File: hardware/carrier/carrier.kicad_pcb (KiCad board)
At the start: 2 copper layers, 117.9 x 72.3 mm, 18 parts, among them J1 12V pigtail, U1 D1 Mini ESP32 (Type-C), U2 PCA9685 16ch servo, U3 LM2596 buck 12V->5.05V

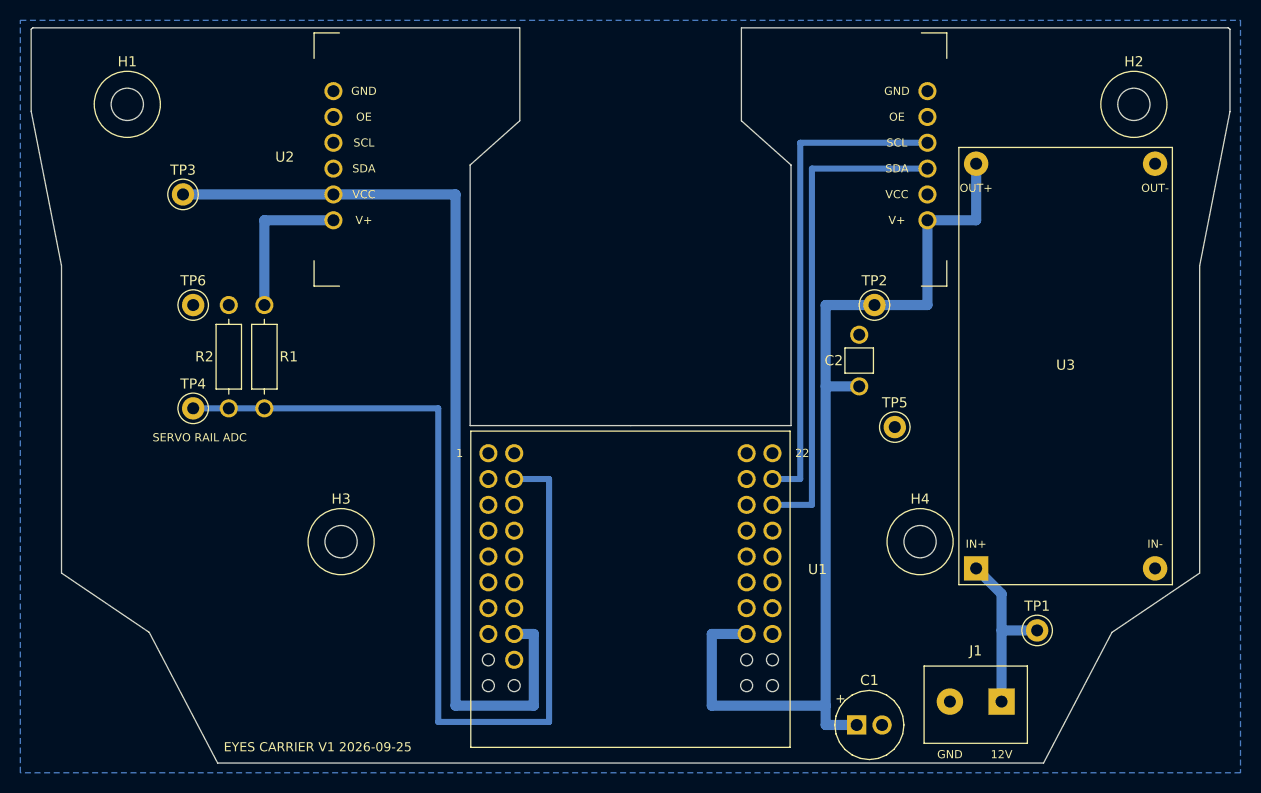
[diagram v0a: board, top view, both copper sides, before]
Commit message: carrier V2: Scott's placement captured, outline restored, divider dropped, DRC 0
PCA on H3/H4 (its holes match the carrier's), D1 Mini in the left wing
with USB-C off the left edge, buck in the right wing, servo headers on
the bottom edge. No routing yet; V1's tracks belonged to the rejected
placement and are gone.

Why a capture step (gen/capture_placement.py -> placement.py) instead of
making the .kicad_pcb the master: the GUI-only path broke the outline
within one session (loose Edge.Cuts lines move under box-select) and
placed three parts off the real board. Regenerating keeps the DXF
outline, hole keepouts and D1 keepouts correct by construction.

Why the hole footprint lost its courtyard and silk ring, and the PCA
courtyard shrank to its header rows: the holes sit inside the PCA by
design; every DRC courtyard check was describing the intent.

Why solid pour connections on U2 pins 6/12 and U3 pins 2/4: servo and
buck return current, and the H3/H4 keepout leaves the PCA GND pins a
single 0.5 mm spoke. Everything else keeps thermal reliefs.

Why min_resolved_spokes 1: the D1's inner GND pin can only be reached
from the module middle; its other two GND pins carry the return.

Rail divider (R1/R2/TP4) removed per Scott: the ADC measured its own
noise, not sag.

Co-Authored-By: Claude Fable 5.1 <noreply@anthropic.com>
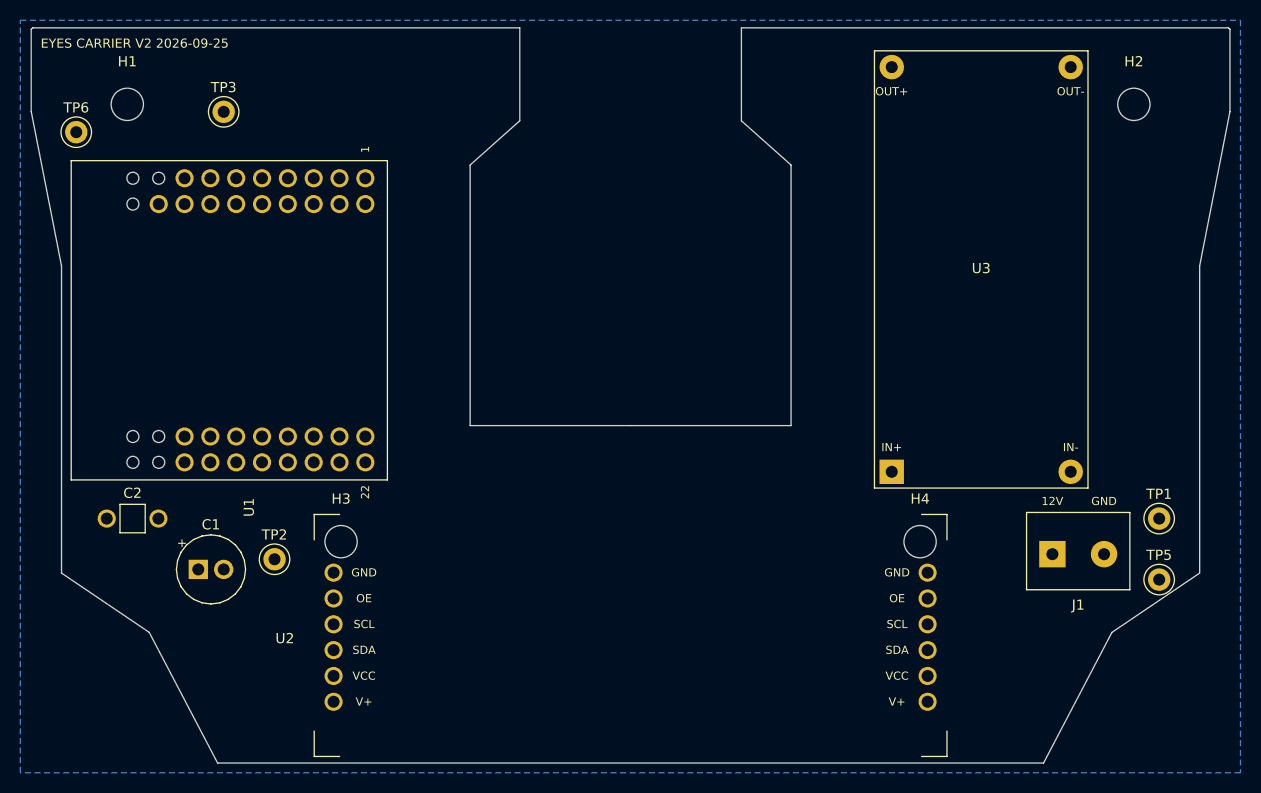
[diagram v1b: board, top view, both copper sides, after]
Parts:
- removed the H4 at (128.5, 115.3)
- removed R1, R2: 10k, carrier:R_Axial_P10.16
- removed the U1 at (100.0, 118.0)
- added U2: PCA9685 16ch servo, carrier:PCA9685_Adafruit_Module, F.Cu at (100.0, 124.8)
- H4: renamed from TP4; value RAIL_ADC -> M3 rack standoff; footprint carrier:TestPoint_THT_D2.2_1.181 -> carrier:MountingHole_M3_3.175
- U1: renamed from U2; value PCA9685 16ch servo -> D1 Mini ESP32 (Type-C); footprint carrier:PCA9685_Adafruit_Module -> carrier:D1_Mini_ESP32_THT
- moved C2 75.1 mm to (48.5, 113.0), turned to 0 degrees
- moved H4 72.7 mm to (128.5, 115.3)
- moved C1 66.5 mm to (57.5, 118.0)
- moved TP2 64.1 mm to (65.0, 117.0)
- moved U1 40.8 mm to (62.5, 93.5), turned to -90 degrees
- moved TP5 30.0 mm to (152.0, 119.0)
- moved TP6 20.5 mm to (45.5, 75.0)
- moved TP1 16.3 mm to (152.0, 113.0)
- moved J1 15.3 mm to (141.5, 116.5), turned to 0 degrees
- moved U3 12.6 mm to (143.3, 108.4)
- moved TP3 9.05 mm to (60.0, 73.0)
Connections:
- U1 pad 1: +5V -> GND
- U1 pad 10: SCL -> (no net)
- U1 pad 12: GND -> (no net)
- U1 pad 2: +3V3 -> (no net)
- U1 pad 6: GND -> (no net)
- U1 pad 7: +5V -> (no net)
- U1 pad 9: SDA -> (no net)
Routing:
- net +5V: track 113.2 -> 0.00 mm
- net +3V3: track 93.8 -> 0.00 mm
- net RAIL_ADC: track 93.2 -> 0.00 mm
- net SDA: track 48.3 -> 0.00 mm
- net SCL: track 48.3 -> 0.00 mm
- net +12V: track 17.6 -> 0.00 mm
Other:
- board text added: "EYES CARRIER V2 2026-09-25"
- board text removed: "EYES CARRIER V1 2026-09-25"
- board text removed: "SERVO RAIL ADC"

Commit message: carrier: 12 V terminal to the right edge mid-depth (Scott) for a panel-mount barrel jack
Wire-entry face toward the edge; the pin labels and ref moved inside the
KF301 body because outside it they were past the board edge. Alternative
rejected: a PCB-mount jack — the one Scott has is panel mount with solder
lugs, so the board only needs a terminal for two wires.

Co-Authored-By: Claude Fable 5.1 <noreply@anthropic.com>
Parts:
- J1: value 12V pigtail -> 12V in
- moved TP1 18.1 mm to (150.5, 95.0)
- moved J1 17.1 mm to (150.5, 102.0), turned to -90 degrees
- moved TP5 5.70 mm to (150.5, 113.5)
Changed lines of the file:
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@@
 	(footprint "carrier:TestPoint_THT_D2.2_1.181"
 		(layer "F.Cu")
-		(at 152 113)
+		(at 150.5 95)
 		(descr "Drilled test point, 2.2 pad on the 1.181 bit (0.51 annulus)")
 		(property "Reference" "TP1"
@@
 	(footprint "carrier:TestPoint_THT_D2.2_1.181"
 		(layer "F.Cu")
-		(at 152 119)
+		(at 150.5 113.5)
 		(descr "Drilled test point, 2.2 pad on the 1.181 bit (0.51 annulus)")
 		(property "Reference" "TP5"
@@
 	(footprint "carrier:KF301_1x02_P5.08"
 		(layer "F.Cu")
-		(at 141.5 116.5)
+		(at 150.5 102 -90)
 		(descr "KF301-5.0 screw terminal 2P 5.08 mm, pads 2.6/1.181")
 		(property "Reference" "J1"
-			(at 2.54 5 0)
+			(at 2.54 -2.4 270)
 			(layer "F.SilkS")
 			(effects
@@
 			)
 		)
-		(property "Value" "12V pigtail"
-			(at 2.54 0 0)
+		(property "Value" "12V in"
+			(at 2.54 0 270)
 			(layer "F.Fab")
 			(effects
@@
 		)
 		(property "Datasheet" ""
-			(at 0 0 0)
+			(at 0 0 270)
 			(layer "F.Fab")
 			(hide yes)
@@
 		)
 		(property "Description" "KF301-5.0 screw terminal 2P 5.08 mm, pads 2.6/1.181"
-			(at 0 0 0)
+			(at 0 0 270)
 			(layer "F.Fab")
 			(hide yes)
@@
 		(duplicate_pad_numbers_are_jumpers no)
 		(fp_line
+			(start -2.54 3.5)
+			(end -2.54 -4.1)
+			(stroke
+				(width 0.12)
+				(type solid)
+			)
+			(layer "F.SilkS")
+		)
+		(fp_line
+			(start 7.62 3.5)
+			(end -2.54 3.5)
+			(stroke
+				(width 0.12)
+				(type solid)
+			)
+			(layer "F.SilkS")
+		)
+		(fp_line
 			(start -2.54 -4.1)
 			(end 7.62 -4.1)
@@
 		)
 		(fp_line
+			(start 7.62 -4.1)
+			(end 7.62 3.5)
+			(stroke
+				(width 0.12)
+				(type solid)
+			)
+			(layer "F.SilkS")
+		)
+		(fp_line
+			(start -2.8 3.8)
+			(end -2.8 -4.4)
+			(stroke
+				(width 0.05)
+				(type solid)
+			)
+			(layer "F.CrtYd")
+		)
+		(fp_line
+			(start 7.9 3.8)
+			(end -2.8 3.8)
+			(stroke
+				(width 0.05)
+				(type solid)
+			)
+			(layer "F.CrtYd")
+		)
+		(fp_line
+			(start -2.8 -4.4)
+			(end 7.9 -4.4)
+			(stroke
+				(width 0.05)
+				(type solid)
+			)
+			(layer "F.CrtYd")
+		)
+		(fp_line
+			(start 7.9 -4.4)
+			(end 7.9 3.8)
+			(stroke
+				(width 0.05)
+				(type solid)
+			)
+			(layer "F.CrtYd")
+		)
+		(fp_line
 			(start -2.54 3.5)
 			(end -2.54 -4.1)
 			(stroke
-				(width 0.12)
-				(type solid)
-			)
-			(layer "F.SilkS")
+				(width 0.1)
+				(type solid)
+			)
+			(layer "F.Fab")
+		)
+		(fp_line
+			(start 7.62 3.5)
+			(end -2.54 3.5)
+			(stroke
+				(width 0.1)
+				(type solid)
+			)
+			(layer "F.Fab")
+		)
+		(fp_line
+			(start -2.54 -4.1)
+			(end 7.62 -4.1)
+			(stroke
+				(width 0.1)
+				(type solid)
+			)
+			(layer "F.Fab")
 		)
 		(fp_line
@@
 			(end 7.62 3.5)
 			(stroke
-				(width 0.12)
-				(type solid)
-			)
-			(layer "F.SilkS")
-		)
-		(fp_line
-			(start 7.62 3.5)
-			(end -2.54 3.5)
-			(stroke
-				(width 0.12)
-				(type solid)
-			)
-			(layer "F.SilkS")
-		)
-		(fp_line
-			(start -2.8 -4.4)
-			(end 7.9 -4.4)
-			(stroke
-				(width 0.05)
-				(type solid)
-			)
-			(layer "F.CrtYd")
-		)
-		(fp_line
-			(start -2.8 3.8)
-			(end -2.8 -4.4)
-			(stroke
-				(width 0.05)
-				(type solid)
-			)
-			(layer "F.CrtYd")
-		)
-		(fp_line
-			(start 7.9 -4.4)
-			(end 7.9 3.8)
-			(stroke
-				(width 0.05)
-				(type solid)
-			)
-			(layer "F.CrtYd")
-		)
-		(fp_line
-			(start 7.9 3.8)
-			(end -2.8 3.8)
-			(stroke
-				(width 0.05)
-				(type solid)
-			)
-			(layer "F.CrtYd")
-		)
-		(fp_line
-			(start -2.54 -4.1)
-			(end 7.62 -4.1)
-			(stroke
-				(width 0.1)
-				(type solid)
-			)
-			(layer "F.Fab")
-		)
-		(fp_line
-			(start -2.54 3.5)
-			(end -2.54 -4.1)
-			(stroke
-				(width 0.1)
-				(type solid)
-			)
-			(layer "F.Fab")
-		)
-		(fp_line
-			(start 7.62 -4.1)
-			(end 7.62 3.5)
-			(stroke
-				(width 0.1)
-				(type solid)
-			)
-			(layer "F.Fab")
-		)
-		(fp_line
-			(start 7.62 3.5)
-			(end -2.54 3.5)
-			(stroke
 				(width 0.1)
 				(type solid)
@@
 		)
 		(fp_text user "12V"
-			(at 0 -5.2 0)
+			(at 0 2.4 270)
 			(layer "F.SilkS")
 			(effects
@@
 		)
 		(fp_text user "GND"
-			(at 5.08 -5.2 0)
+			(at 5.08 2.4 270)
 			(layer "F.SilkS")
 			(effects
@@
 		)
 		(pad "1" thru_hole rect
-			(at 0 0)
+			(at 0 0 270)
 			(size 2.6 2.6)
 			(drill 1.181)
@@
 		)
 		(pad "2" thru_hole circle
-			(at 5.08 0)
+			(at 5.08 0 270)
 			(size 2.6 2.6)
 			(drill 1.181)
